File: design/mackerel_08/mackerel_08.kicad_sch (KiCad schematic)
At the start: 13 parts, among them U1 MC68008FN, X1 CXO_DIP14

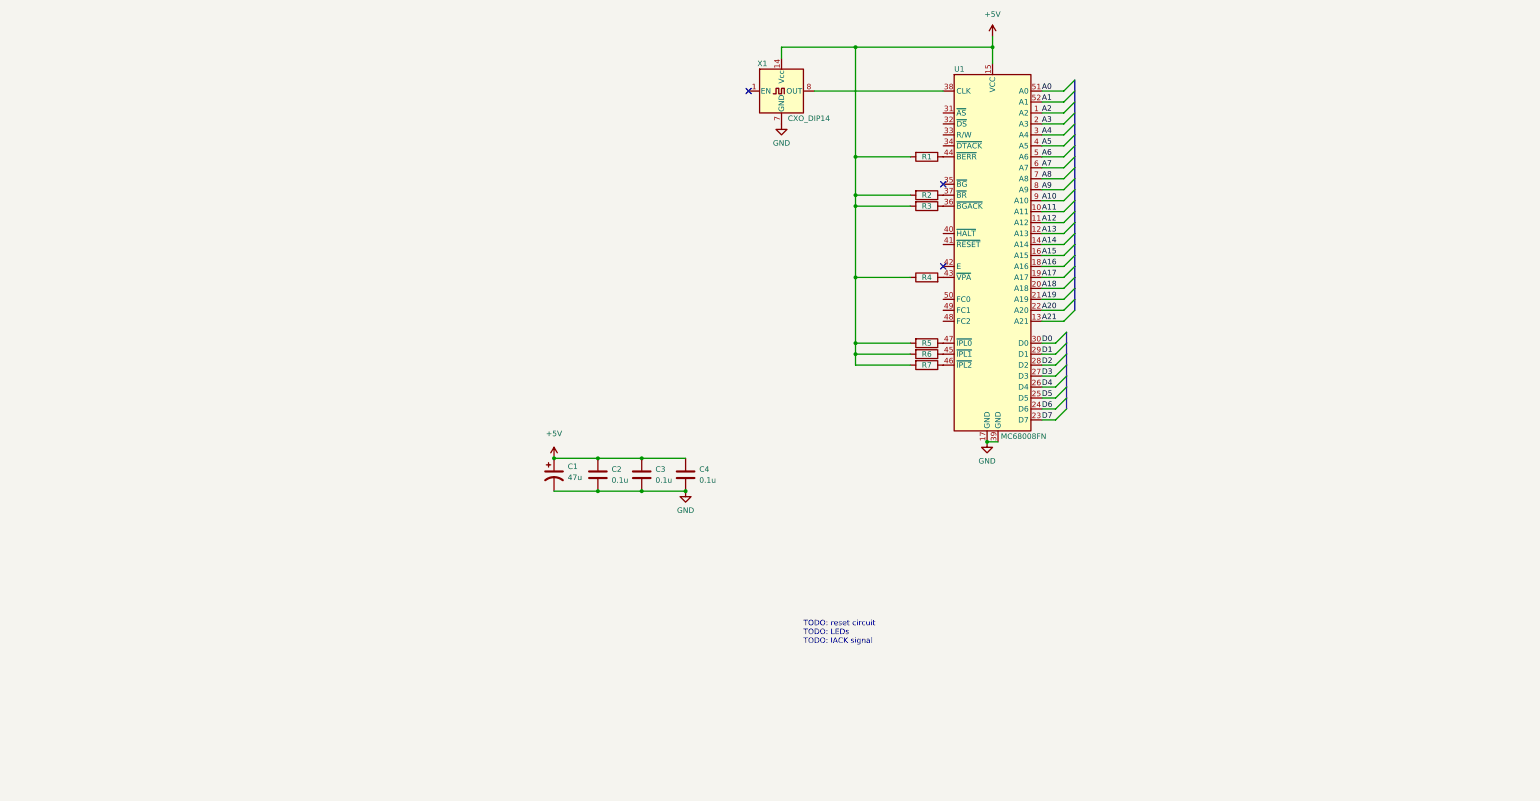
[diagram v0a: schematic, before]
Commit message: CPU and decoder board schematic in progress
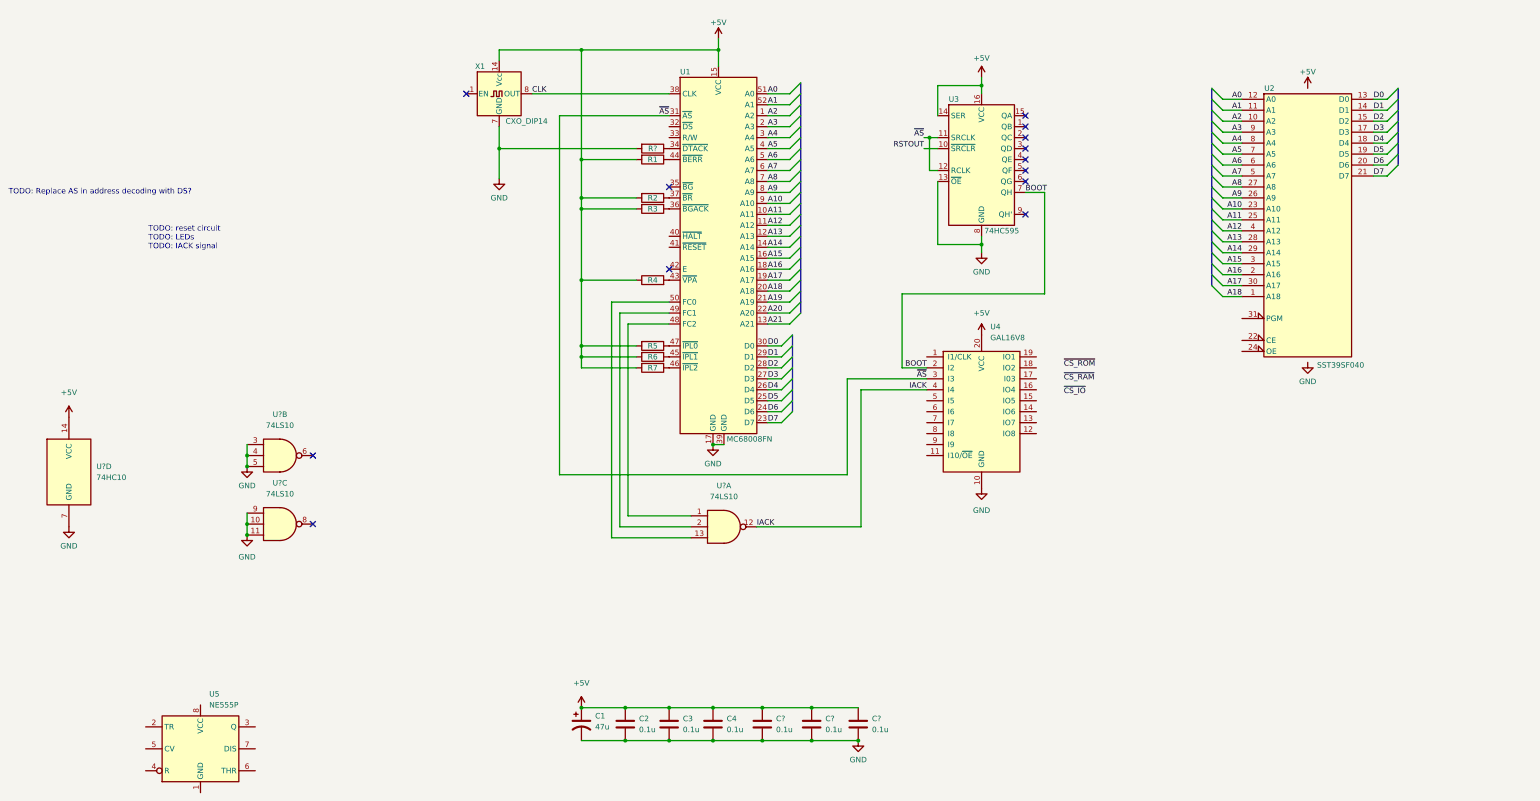
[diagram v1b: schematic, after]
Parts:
- added C? (x3): 0.1u, Capacitor_THT:C_Disc_D4.3mm_W1.9mm_P5.00mm, symbol Device:C
- added R?: 4k7, Resistor_THT:R_Axial_DIN0207_L6.3mm_D2.5mm_P10.16mm_Horizontal, symbol Device:R
- added U2: SST39SF040, Package_DIP:DIP-32_W15.24mm_Socket, symbol Memory_Flash:SST39SF040
- added U3: 74HC595, Package_DIP:DIP-16_W7.62mm_Socket, symbol 74xx:74HC595
- added U4: GAL16V8, symbol Logic_Programmable:GAL16V8
- added U5: NE555P, Package_DIP:DIP-8_W7.62mm_Socket, symbol Timer:NE555P
- added U? (x3): 74LS10, symbol 74xx:74LS10
- added U?: 74HC10, symbol 74xx:74LS10
- C1: footprint (none) -> Capacitor_THT:CP_Radial_D5.0mm_P2.50mm
- C2, C3, C4: footprint (none) -> Capacitor_THT:C_Disc_D4.3mm_W1.9mm_P5.00mm
- R1, R2, R3, R4, R5, R6, R7: footprint (none) -> Resistor_THT:R_Axial_DIN0207_L6.3mm_D2.5mm_P10.16mm_Horizontal
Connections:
- net +5V: now also C?.1, C?.1, C?.1, U2.32 (VCC), U3.14 (SER), U3.16 (VCC), U4.20 (VCC), U?.14 (VCC)
- net A0: now also U2.12 (A0)
- net A1: now also U2.11 (A1)
- net A10: now also U2.23 (A10)
- net A11: now also U2.25 (A11)
- net A12: now also U2.4 (A12)
- net A13: now also U2.28 (A13)
- net A14: now also U2.29 (A14)
- net A15: now also U2.3 (A15)
- net A16: now also U2.2 (A16)
- net A17: now also U2.30 (A17)
- net A18: now also U2.1 (A18)
- net A2: now also U2.10 (A2)
- net A3: now also U2.9 (A3)
- net A4: now also U2.8 (A4)
- net A5: now also U2.7 (A5)
- net A6: now also U2.6 (A6)
- net A7: now also U2.5 (A7)
- net A8: now also U2.27 (A8)
- net A9: now also U2.26 (A9)
- net D0: now also U2.13 (D0)
- net D1: now also U2.14 (D1)
- net D2: now also U2.15 (D2)
- net D3: now also U2.17 (D3)
- net D4: now also U2.18 (D4)
- net D5: now also U2.19 (D5)
- net D6: now also U2.20 (D6)
- net D7: now also U2.21 (D7)
- net GND: now also C?.2, C?.2, C?.2, R?.2, U2.16 (GND), U3.13 (~{OE}), U3.8 (GND), U4.10 (GND), U?.10, U?.11, U?.3, U?.4, U?.5, U?.7 (GND), U?.9
- net ~{AS}: now reaches U1.31 (~{AS})
- net ~{AS}: now also U3.11 (SRCLK), U3.12 (RCLK), U4.3 (I3)
- net at U1.34 (~{DTACK}): now also R?.1
- net CLK: now reaches U1.38 (CLK), X1.8 (OUT)
- net at U1.48 (FC2): now also U?.1
- net at U1.49 (FC1): now also U?.2
- net at U1.50 (FC0): now also U?.13
- new net BOOT: U3.7 (QH), U4.2 (I2)
- new net IACK: U4.4 (I4), U?.12
- new net RSTOUT: U3.10 (~{SRCLR})
- no-connect marks 3 -> 13
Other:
- note added: "TODO: Replace AS in address decoding with DS?"
- moved on the sheet: C1, C2, C3, C4, R1, R2, R3, R4, R5, R6, R7, U1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

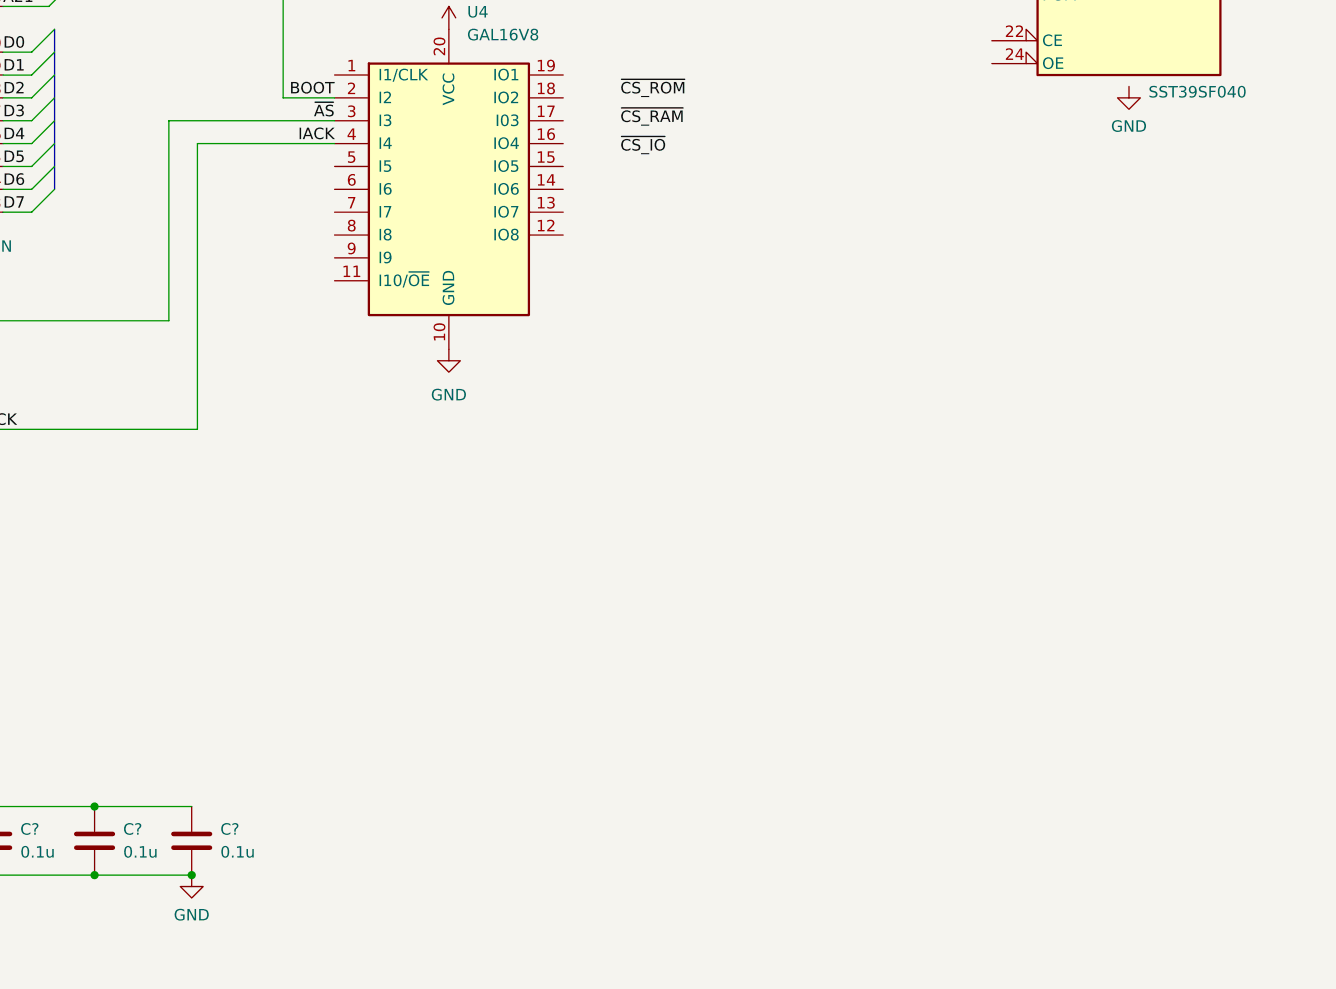
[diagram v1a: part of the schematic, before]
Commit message: Stubbed out IACK and DTACK PLDs in schematic
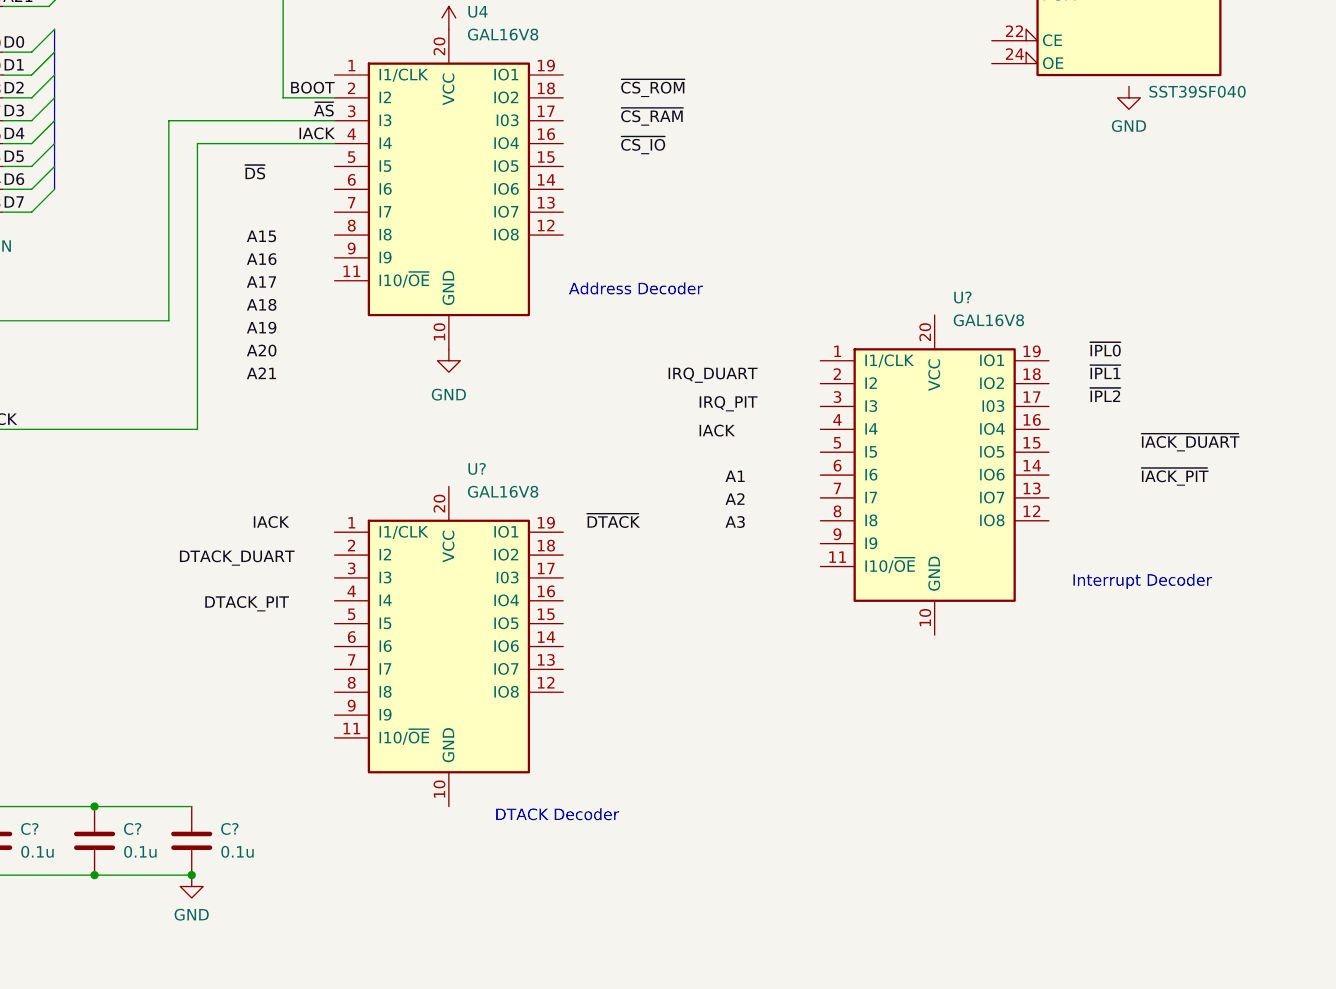
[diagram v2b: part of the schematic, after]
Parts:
- added U? (x2): GAL16V8, Package_DIP:DIP-20_W7.62mm_Socket, symbol Logic_Programmable:GAL16V8
- U4: footprint (none) -> Package_DIP:DIP-20_W7.62mm_Socket
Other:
- note added: "Address Decoder"
- note added: "DTACK Decoder"
- note added: "Interrupt Decoder"
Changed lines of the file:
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@@
+    (effects (font (size 1.27 1.27)) (justify left bottom))
+  )
+  (text "Address Decoder" (at 147.32 120.015 0)
+    (effects (font (size 1.27 1.27)) (justify left bottom))
+  )
+  (text "Interrupt Decoder" (at 203.2 152.4 0)
     (effects (font (size 1.27 1.27)) (justify left bottom))
   )
@@
     (effects (font (size 1.27 1.27)) (justify left bottom))
   )
+  (text "DTACK Decoder" (at 139.065 178.435 0)
+    (effects (font (size 1.27 1.27)) (justify left bottom))
+  )
   (label "A5" (at 84.455 46.99 0)
     (effects (font (size 1.27 1.27)) (justify left bottom))
@@
     (effects (font (size 1.27 1.27)) (justify left bottom))
   )
+  (label "IACK" (at 165.735 135.89 180)
+    (effects (font (size 1.27 1.27)) (justify right bottom))
+  )
   (label "A9" (at 84.455 57.15 0)
     (effects (font (size 1.27 1.27)) (justify left bottom))
@@
     (effects (font (size 1.27 1.27)) (justify left bottom))
   )
+  (label "DTACK_PIT" (at 116.205 154.94 180)
+    (effects (font (size 1.27 1.27)) (justify right bottom))
+  )
+  (label "~{IPL0}" (at 205.105 127 0)
+    (effects (font (size 1.27 1.27)) (justify left bottom))
+  )
   (label "A1" (at 84.455 36.83 0)
     (effects (font (size 1.27 1.27)) (justify left bottom))
@@
     (effects (font (size 1.27 1.27)) (justify left bottom))
   )
+  (label "A15" (at 114.935 114.3 180)
+    (effects (font (size 1.27 1.27)) (justify right bottom))
+  )
   (label "A17" (at 194.31 78.74 180)
     (effects (font (size 1.27 1.27)) (justify right bottom))
@@
     (effects (font (size 1.27 1.27)) (justify right bottom))
   )
+  (label "~{IPL1}" (at 205.105 129.54 0)
+    (effects (font (size 1.27 1.27)) (justify left bottom))
+  )
   (label "~{CS_ROM}" (at 153.035 97.79 0)
     (effects (font (size 1.27 1.27)) (justify left bottom))
@@
     (effects (font (size 1.27 1.27)) (justify left bottom))
   )
+  (label "A1" (at 167.005 140.97 180)
+    (effects (font (size 1.27 1.27)) (justify right bottom))
+  )
   (label "D6" (at 224.79 50.8 0)
     (effects (font (size 1.27 1.27)) (justify left bottom))
   )
+  (label "A18" (at 114.935 121.92 180)
+    (effects (font (size 1.27 1.27)) (justify right bottom))
+  )
   (label "D4" (at 84.455 102.87 0)
     (effects (font (size 1.27 1.27)) (justify left bottom))
@@
     (effects (font (size 1.27 1.27)) (justify right bottom))
   )
+  (label "~{IPL2}" (at 205.105 132.08 0)
+    (effects (font (size 1.27 1.27)) (justify left bottom))
+  )
   (label "A12" (at 84.455 64.77 0)
     (effects (font (size 1.27 1.27)) (justify left bottom))
@@
     (effects (font (size 1.27 1.27)) (justify right bottom))
   )
+  (label "~{IACK_PIT}" (at 210.82 140.97 0)
+    (effects (font (size 1.27 1.27)) (justify left bottom))
+  )
   (label "A1" (at 194.31 38.1 180)
     (effects (font (size 1.27 1.27)) (justify right bottom))
@@
     (effects (font (size 1.27 1.27)) (justify left bottom))
   )
+  (label "~{DTACK}" (at 149.225 146.05 0)
+    (effects (font (size 1.27 1.27)) (justify left bottom))
+  )
   (label "A15" (at 84.455 72.39 0)
     (effects (font (size 1.27 1.27)) (justify left bottom))
@@
     (effects (font (size 1.27 1.27)) (justify left bottom))
   )
+  (label "IRQ_DUART" (at 168.275 129.54 180)
+    (effects (font (size 1.27 1.27)) (justify right bottom))
+  )
   (label "A6" (at 194.31 50.8 180)
     (effects (font (size 1.27 1.27)) (justify right bottom))
@@
     (effects (font (size 1.27 1.27)) (justify left bottom))
   )
+  (label "~{IACK_DUART}" (at 210.82 137.16 0)
+    (effects (font (size 1.27 1.27)) (justify left bottom))
+  )
+  (label "DTACK_DUART" (at 116.84 149.86 180)
+    (effects (font (size 1.27 1.27)) (justify right bottom))
+  )
   (label "~{CS_RAM}" (at 153.035 100.965 0)
     (effects (font (size 1.27 1.27)) (justify left bottom))
@@
     (effects (font (size 1.27 1.27)) (justify left bottom))
   )
+  (label "IACK" (at 116.205 146.05 180)
+    (effects (font (size 1.27 1.27)) (justify right bottom))
+  )
+  (label "IRQ_PIT" (at 168.275 132.715 180)
+    (effects (font (size 1.27 1.27)) (justify right bottom))
+  )
+  (label "~{DS}" (at 113.665 107.315 180)
+    (effects (font (size 1.27 1.27)) (justify right bottom))
+  )
+  (label "A19" (at 114.935 124.46 180)
+    (effects (font (size 1.27 1.27)) (justify right bottom))
+  )
   (label "A15" (at 194.31 73.66 180)
     (effects (font (size 1.27 1.27)) (justify right bottom))
@@
     (effects (font (size 1.27 1.27)) (justify right bottom))
   )
+  (label "A21" (at 114.935 129.54 180)
+    (effects (font (size 1.27 1.27)) (justify right bottom))
+  )
+  (label "A17" (at 114.935 119.38 180)
+    (effects (font (size 1.27 1.27)) (justify right bottom))
+  )
+  (label "A16" (at 114.935 116.84 180)
+    (effects (font (size 1.27 1.27)) (justify right bottom))
+  )
   (label "A14" (at 84.455 69.85 0)
     (effects (font (size 1.27 1.27)) (justify left bottom))
@@
     (effects (font (size 1.27 1.27)) (justify right bottom))
   )
+  (label "A20" (at 114.935 127 180)
+    (effects (font (size 1.27 1.27)) (justify right bottom))
+  )
   (label "BOOT" (at 144.145 57.15 0)
     (effects (font (size 1.27 1.27)) (justify left bottom))
   )
+  (label "A3" (at 167.005 146.05 180)
+    (effects (font (size 1.27 1.27)) (justify right bottom))
+  )
   (label "D2" (at 224.79 40.64 0)
     (effects (font (size 1.27 1.27)) (justify left bottom))
+  )
+  (label "A2" (at 167.005 143.51 180)
+    (effects (font (size 1.27 1.27)) (justify right bottom))
   )
   (symbol (lib_id "74xx:74LS10") (at -28.575 133.985 0) (unit 3)
@@
     (pin "1")
   )
+  (symbol (lib_id "Logic_Programmable:GAL16V8") (at 133.985 158.75 0) (unit 1)
+    (in_bom yes) (on_board yes) (fields_autoplaced)
+    (property "Reference" "U?" (id 0) (at 136.0044 139.065 0)
+      (effects (font (size 1.27 1.27)) (justify left))
+    )
+    (property "Value" "GAL16V8" (id 1) (at 136.0044 141.605 0)
+      (effects (font (size 1.27 1.27)) (justify left))
+    )
+    (property "Footprint" "Package_DIP:DIP-20_W7.62mm_Socket" (id 2) (at 133.985 158.75 0)
+      (effects (font (size 1.27 1.27)) hide)
+    )
+    (property "Datasheet" "" (id 3) (at 133.985 158.75 0)
+      (effects (font (size 1.27 1.27)) hide)
+    )
+    (pin "10")
+    (pin "20")
+    (pin "1")
+    (pin "11")
+    (pin "12")
+    (pin "13")
+    (pin "14")
+    (pin "15")
+    (pin "16")
+    (pin "17")
+    (pin "18")
+    (pin "19")
+    (pin "2")
+    (pin "3")
+    (pin "4")
+    (pin "5")
+    (pin "6")
+    (pin "7")
+    (pin "8")
+    (pin "9")
+  )
   (symbol (lib_id "power:+5V") (at 133.985 90.17 0) (unit 1)
     (in_bom yes) (on_board yes) (fields_autoplaced)
@@
       (effects (font (size 1.27 1.27)) (justify left))
     )
-    (property "Footprint" "" (id 2) (at 133.985 107.95 0)
+    (property "Footprint" "Package_DIP:DIP-20_W7.62mm_Socket" (id 2) (at 133.985 107.95 0)
       (effects (font (size 1.27 1.27)) hide)
     )
@@
     (pin "7")
   )
+  (symbol (lib_id "Logic_Programmable:GAL16V8") (at 187.96 139.7 0) (unit 1)
+    (in_bom yes) (on_board yes) (fields_autoplaced)
+    (property "Reference" "U?" (id 0) (at 189.9794 120.015 0)
+      (effects (font (size 1.27 1.27)) (justify left))
+    )
+    (property "Value" "GAL16V8" (id 1) (at 189.9794 122.555 0)
+      (effects (font (size 1.27 1.27)) (justify left))
+    )
+    (property "Footprint" "Package_DIP:DIP-20_W7.62mm_Socket" (id 2) (at 187.96 139.7 0)
+      (effects (font (size 1.27 1.27)) hide)
+    )
+    (property "Datasheet" "" (id 3) (at 187.96 139.7 0)
+      (effects (font (size 1.27 1.27)) hide)
+    )
+    (pin "10")
+    (pin "20")
+    (pin "1")
+    (pin "11")
+    (pin "12")
+    (pin "13")
+    (pin "14")
+    (pin "15")
+    (pin "16")
+    (pin "17")
+    (pin "18")
+    (pin "19")
+    (pin "2")
+    (pin "3")
+    (pin "4")
+    (pin "5")
+    (pin "6")
+    (pin "7")
+    (pin "8")
+    (pin "9")
+  )
   (symbol (lib_id "power:+5V") (at 209.55 33.02 0) (unit 1)
     (in_bom yes) (on_board yes)
@@
       (reference "U5") (unit 1) (value "NE555P") (footprint "Package_DIP:DIP-8_W7.62mm_Socket")
     )
+    (path "/23a07234-2627-4889-a1e0-db01fa7550a8"
+      (reference "U?") (unit 1) (value "GAL16V8") (footprint "Package_DIP:DIP-20_W7.62mm_Socket")
+    )
     (path "/8433cabe-e95e-4ffa-b3c4-e5f988cc9f59"
       (reference "U?") (unit 1) (value "74LS10") (footprint "")
     )
+    (path "/85fc2c7a-f835-49fb-bc62-2a0db8d97a38"
+      (reference "U?") (unit 1) (value "GAL16V8") (footprint "Package_DIP:DIP-20_W7.62mm_Socket")
+    )
     (path "/b6ed6e3f-98bf-409a-904c-99a2a4de8150"
